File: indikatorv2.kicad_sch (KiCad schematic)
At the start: 61 parts, among them U1 XIAO-ESP32-C3-SMD

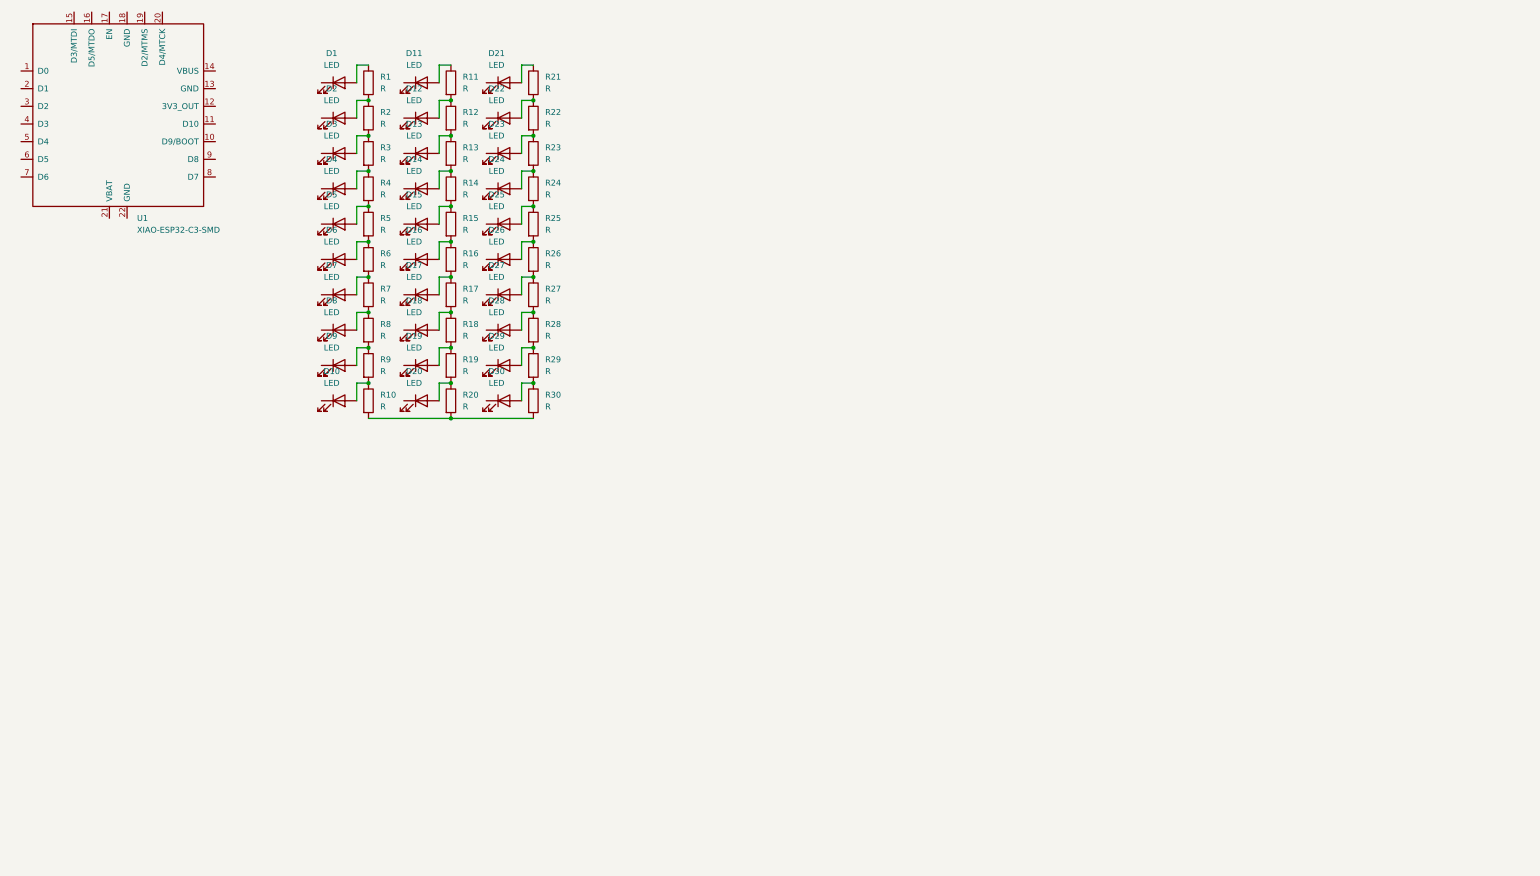
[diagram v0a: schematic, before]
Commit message: connect all leds and mosfets ig, still need to do all the battery stuff
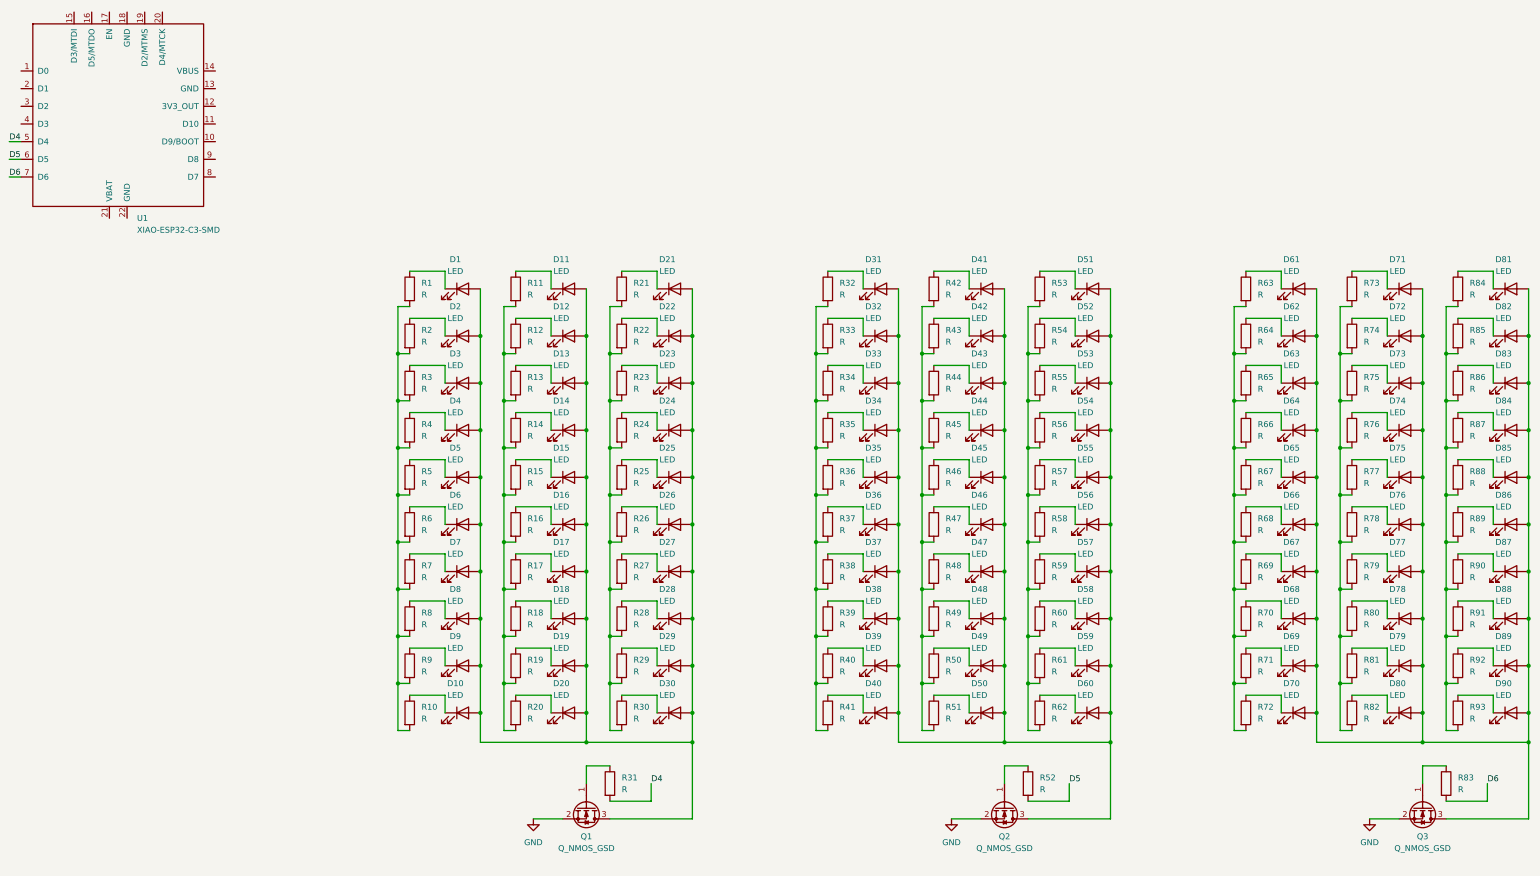
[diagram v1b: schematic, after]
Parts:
- added D31, D32, D33, D34, D35, D36, D37, D38, D39, D40, D41, D42, D43, D44, D45, D46, D47, D48, D49, D50, D51, D52, D53, D54, D55, D56, D57, D58, D59, D60, D61, D62, D63, D64, D65, D66, D67, D68, D69, D70, D71, D72, D73, D74, D75, D76, D77, D78, D79, D80, D81, D82, D83, D84, D85, D86, D87, D88, D89, D90: LED, LED_SMD:LED_Cree-XHP50_3V_HighDensity, symbol Device:LED
- added Q1, Q2, Q3: Q_NMOS_GSD, Converter_DCDC:Converter_DCDC_XP_POWER-IAxxxxD_THT, symbol Transistor_FET:Q_NMOS_GSD
- added R31, R32, R33, R34, R35, R36, R37, R38, R39, R40, R41, R42, R43, R44, R45, R46, R47, R48, R49, R50, R51, R52, R53, R54, R55, R56, R57, R58, R59, R60, R61, R62, R63, R64, R65, R66, R67, R68, R69, R70, R71, R72, R73, R74, R75, R76, R77, R78, R79, R80, R81, R82, R83, R84, R85, R86, R87, R88, R89, R90, R91, R92, R93: R, Package_BGA:UFBGA-64_5x5mm_Layout8x8_P0.5mm, symbol Device:R
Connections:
- net at D28.1 (K): now also R28.1
- net at D24.1 (K): now also R24.1
- net at D1.2 (A): now also D10.2 (A), D11.2 (A), D12.2 (A), D13.2 (A), D14.2 (A), D15.2 (A), D16.2 (A), D17.2 (A), D18.2 (A), D19.2 (A), D2.2 (A), D20.2 (A), D21.2 (A), D22.2 (A), D23.2 (A), D24.2 (A), D25.2 (A), D26.2 (A), D27.2 (A), D28.2 (A), D29.2 (A), D3.2 (A), D30.2 (A), D4.2 (A), D5.2 (A), D6.2 (A), D7.2 (A), D8.2 (A), D9.2 (A), Q1.3 (D); no longer R1.1
- net at D6.1 (K): now also R6.1
- net at D30.1 (K): now also R30.1
- net at D5.1 (K): now also R5.1
- net at D4.1 (K): now also R4.1
- net D4: now reaches U1.5 (D4)
- net D4: now also R31.2
- net D5: now reaches U1.6 (D5)
- net D5: now also R52.2
- net D6: now reaches U1.7 (D6)
- net D6: now also R83.2
- net at R21.1: now also D21.1 (K); no longer D21.2 (A)
- net at D9.1 (K): now also R9.1
- net at D3.1 (K): now also R3.1
- net at D1.1 (K): now also R1.1
- net at D19.1 (K): now also R19.1
- net at D11.1 (K): now also R11.1
- net at D22.1 (K): now also R22.1
- net at D23.1 (K): now also R23.1
- net at D26.1 (K): now also R26.1
- net at D8.1 (K): now also R8.1
- net at D20.1 (K): now also R20.1
- net at D2.1 (K): now also R2.1
- net at D7.1 (K): now also R7.1
- net at D17.1 (K): now also R17.1
- net at D27.1 (K): now also R27.1
- net at D15.1 (K): now also R15.1
- net at D13.1 (K): now also R13.1
- net at D18.1 (K): now also R18.1
- net at D12.1 (K): now also R12.1
- net at D29.1 (K): now also R29.1
- net at D14.1 (K): now also R14.1
- net at D16.1 (K): now also R16.1
- net at D25.1 (K): now also R25.1
- net at D10.1 (K): now also R10.1
- new net: D86.1 (K), R89.1
- new net: D61.2 (A), D62.2 (A), D63.2 (A), D64.2 (A), D65.2 (A), D66.2 (A), D67.2 (A), D68.2 (A), D69.2 (A), D70.2 (A), D71.2 (A), D72.2 (A), D73.2 (A), D74.2 (A), D75.2 (A), D76.2 (A), D77.2 (A), D78.2 (A), D79.2 (A), D80.2 (A), D81.2 (A), D82.2 (A), D83.2 (A), D84.2 (A), D85.2 (A), D86.2 (A), D87.2 (A), D88.2 (A), D89.2 (A), D90.2 (A), Q3.3 (D)
- new net: R11.2, R12.2, R13.2, R14.2, R15.2, R16.2, R17.2, R18.2, R19.2, R20.2
- new net: D43.1 (K), R44.1
- new net: R42.2, R43.2, R44.2, R45.2, R46.2, R47.2, R48.2, R49.2, R50.2, R51.2
- new net: D77.1 (K), R79.1
- new net: D44.1 (K), R45.1
- new net: D31.2 (A), D32.2 (A), D33.2 (A), D34.2 (A), D35.2 (A), D36.2 (A), D37.2 (A), D38.2 (A), D39.2 (A), D40.2 (A), D41.2 (A), D42.2 (A), D43.2 (A), D44.2 (A), D45.2 (A), D46.2 (A), D47.2 (A), D48.2 (A), D49.2 (A), D50.2 (A), D51.2 (A), D52.2 (A), D53.2 (A), D54.2 (A), D55.2 (A), D56.2 (A), D57.2 (A), D58.2 (A), D59.2 (A), D60.2 (A), Q2.3 (D)
- new net: D46.1 (K), R47.1
- new net: D34.1 (K), R35.1
- new net: D76.1 (K), R78.1
- new net: D58.1 (K), R60.1
- new net: R53.2, R54.2, R55.2, R56.2, R57.2, R58.2, R59.2, R60.2, R61.2, R62.2
- new net: R1.2, R10.2, R2.2, R3.2, R4.2, R5.2, R6.2, R7.2, R8.2, R9.2
- new net: D68.1 (K), R70.1
- new net: D57.1 (K), R59.1
- new net: D37.1 (K), R38.1
- new net: D87.1 (K), R90.1
- new net: D49.1 (K), R50.1
- new net: D32.1 (K), R33.1
- new net: D83.1 (K), R86.1
- new net: R84.2, R85.2, R86.2, R87.2, R88.2, R89.2, R90.2, R91.2, R92.2, R93.2
- new net: D75.1 (K), R77.1
- new net: R73.2, R74.2, R75.2, R76.2, R77.2, R78.2, R79.2, R80.2, R81.2, R82.2
- new net: D79.1 (K), R81.1
- new net: D72.1 (K), R74.1
- new net: R32.2, R33.2, R34.2, R35.2, R36.2, R37.2, R38.2, R39.2, R40.2, R41.2
- new net: D31.1 (K), R32.1
- new net: R21.2, R22.2, R23.2, R24.2, R25.2, R26.2, R27.2, R28.2, R29.2, R30.2
- new net: D47.1 (K), R48.1
- new net: D60.1 (K), R62.1
- new net: D78.1 (K), R80.1
- new net: D40.1 (K), R41.1
- new net: D45.1 (K), R46.1
- new net: D48.1 (K), R49.1
- new net: D33.1 (K), R34.1
- new net: D63.1 (K), R65.1
- new net: R63.2, R64.2, R65.2, R66.2, R67.2, R68.2, R69.2, R70.2, R71.2, R72.2
- new net: D50.1 (K), R51.1
- new net: D39.1 (K), R40.1
- new net: D70.1 (K), R72.1
- new net: D56.1 (K), R58.1
- new net: D74.1 (K), R76.1
- new net: D51.1 (K), R53.1
- new net: D53.1 (K), R55.1
- new net: D36.1 (K), R37.1
- new net: D85.1 (K), R88.1
- new net: D59.1 (K), R61.1
- new net: Q1.1 (G), R31.1
- new net: D61.1 (K), R63.1
- new net: D82.1 (K), R85.1
- new net: D66.1 (K), R68.1
- new net: D62.1 (K), R64.1
- new net: D41.1 (K), R42.1
- new net: D52.1 (K), R54.1
- new net: D84.1 (K), R87.1
- new net: D69.1 (K), R71.1
- new net: D64.1 (K), R66.1
- new net: D73.1 (K), R75.1
- new net: D65.1 (K), R67.1
- new net: D81.1 (K), R84.1
- new net: D35.1 (K), R36.1
- new net: D89.1 (K), R92.1
- new net: D42.1 (K), R43.1
- new net: D38.1 (K), R39.1
- new net: D54.1 (K), R56.1
- new net: Q3.1 (G), R83.1
- new net: D90.1 (K), R93.1
- new net: D55.1 (K), R57.1
- new net: D80.1 (K), R82.1
- new net: D71.1 (K), R73.1
- new net: D67.1 (K), R69.1
- new net: Q2.1 (G), R52.1
- new net: D88.1 (K), R91.1
- new net GND: Q1.2 (S), Q2.2 (S), Q3.2 (S)

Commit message: journal
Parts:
- added J1: Conn_01x02_Pin, symbol Connector:Conn_01x02_Pin
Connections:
- new net BAT+: J1.1 (Pin_1)
- new net BAT-: J1.2 (Pin_2)
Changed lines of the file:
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@@
 		)
 	)
+	(label "BAT-"
+		(at 106.68 52.07 0)
+		(effects
+			(font
+				(size 1.27 1.27)
+			)
+			(justify left bottom)
+		)
+	)
 	(label "D5"
 		(at 17.78 54.61 0)
@@
 		)
 	)
+	(label "BAT+"
+		(at 106.68 49.53 0)
+		(effects
+			(font
+				(size 1.27 1.27)
+			)
+			(justify left bottom)
+		)
+	)
 	(label "D6"
 		(at 336.55 189.23 0)
@@
 					(unit 1)
 				)
+			)
+		)
+	)
+	(symbol
+		(lib_id "Connector:Conn_01x02_Pin")
+		(at 101.6 49.53 0)
+		(unit 1)
+		(body_style 1)
+		(exclude_from_sim no)
+		(in_bom yes)
+		(on_board yes)
+		(in_pos_files yes)
+		(dnp no)
+		(fields_autoplaced yes)
+		(property "Reference" "J1"
+			(at 102.235 44.45 0)
+			(show_name no)
+			(do_not_autoplace no)
+			(effects
+				(font
+					(size 1.27 1.27)
+				)
+			)
+		)
+		(property "Value" "Conn_01x02_Pin"
+			(at 102.235 46.99 0)
+			(show_name no)
+			(do_not_autoplace no)
+			(effects
+				(font
+					(size 1.27 1.27)
+				)
+			)
+		)
+		(property "Footprint" ""
+			(at 101.6 49.53 0)
+			(hide yes)
+			(show_name no)
+			(do_not_autoplace no)
+			(effects
+				(font
+					(size 1.27 1.27)
+				)
+			)
+		)
+		(property "Datasheet" ""
+			(at 101.6 49.53 0)
+			(hide yes)
+			(show_name no)
+			(do_not_autoplace no)
+			(effects
+				(font
+					(size 1.27 1.27)
+				)
+			)
+		)
+		(property "Description" "Generic connector, single row, 01x02, script generated"
+			(at 101.6 49.53 0)
+			(hide yes)
+			(show_name no)
+			(do_not_autoplace no)
+			(effects
+				(font
+					(size 1.27 1.27)
+				)
+			)
+		)
+		(pin "2"
+		)
+		(pin "1"
+		)
+		(instances
+			(project "indikatorv2"
+				(path "/2add1593-661d-41a8-811f-b5b798956a46"
+					(reference "J1")
+					(unit 1)
+				)

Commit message: do battery stuff
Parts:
- removed R31, R52, R83: R, Package_BGA:UFBGA-64_5x5mm_Layout8x8_P0.5mm, symbol Device:R
- added F1: Fuse, symbol Device:Fuse
- added J2, J3, J4: Conn_01x02_Pin, symbol Connector:Conn_01x02_Pin
- added SW1: SW_SPST, Button_Switch_THT:SW_NKK_GW12LJP, symbol Switch:SW_SPST
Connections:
- net D4: now also Q1.1 (G)
- net D5: now also Q2.1 (G)
- net D6: now also Q3.1 (G)
- net GND: now also U1.22 (GND), J3.2 (Pin_2), J4.2 (Pin_2)
- net BOOST_OUT: now reaches D11.1 (K), R11.1
- net BOOST_OUT: now also D1.1 (K), D21.1 (K), D31.1 (K), D41.1 (K), D51.1 (K), D61.1 (K), D71.1 (K), D81.1 (K), R1.1, R21.1, R32.1, R42.1, R53.1, R63.1, R73.1, R84.1, U1.21 (VBAT), J4.1 (Pin_1)
- new net: F1.2, SW1.1 (A)
- new net BOOST_IN: J3.1 (Pin_1), SW1.2 (B)
- new net PROTECTED+: F1.1, J2.1 (Pin_1)
- new net PROTECTED-: J2.2 (Pin_2)
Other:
- moved on the sheet: D1, D10, D11, D12, D13, D14, D15, D16, D17, D18, D19, D2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

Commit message: create fuse footprint, assign footprints for everything and pass erc
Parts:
- F1: footprint (none) -> components:FuseHolder_ELCOM_PBF-4
- J1, J2, J3, J4: footprint (none) -> TerminalBlock:TerminalBlock_MaiXu_MX126-5.0-02P_1x02_P5.00mm
- R1, R10, R11, R12, R13, R14, R15, R16, R17, R18, R19, R2, R20, R21, R22, R23, R24, R25, R26, R27, R28, R29, R3, R30, R4, R5, R6, R63, R64, R65, R66, R67, R68, R69, R7, R70, R71, R72, R73, R74, R75, R76, R77, R78, R79, R8, R80, R81, R82, R84, R85, R86, R87, R88, R89, R9, R90, R91, R92, R93: value R -> 200; footprint Package_BGA:UFBGA-64_5x5mm_Layout8x8_P0.5mm -> Resistor_SMD:R_0805_2012Metric
- R32, R33, R34, R35, R36, R37, R38, R39, R40, R41, R42, R43, R44, R45, R46, R47, R48, R49, R50, R51, R53, R54, R55, R56, R57, R58, R59, R60, R61, R62: value R -> 300; footprint Package_BGA:UFBGA-64_5x5mm_Layout8x8_P0.5mm -> Resistor_SMD:R_0805_2012Metric
- U1: footprint Seeed_Studio_XIAO_Series:XIAO-ESP32-C3-SMD -> RF_Module:MCU_Seeed_ESP32C3
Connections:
- no-connect marks 0 -> 17
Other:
- moved on the sheet: U1

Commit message: i tried okay, also journal
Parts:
- D1, D10, D11, D12, D13, D14, D15, D16, D17, D18, D19, D2, D20, D21, D22, D23, D24, D25, D26, D27, D28, D29, D3, D30, D31, D32, D33, D34, D35, D36, D37, D38, D39, D4, D40, D41, D42, D43, D44, D45, D46, D47, D48, D49, D5, D50, D51, D52, D53, D54, D55, D56, D57, D58, D59, D6, D60, D61, D62, D63, D64, D65, D66, D67, D68, D69, D7, D70, D71, D72, D73, D74, D75, D76, D77, D78, D79, D8, D80, D81, D82, D83, D84, D85, D86, D87, D88, D89, D9, D90: footprint LED_SMD:LED_Cree-XHP50_3V_HighDensity -> components:L128-CLR1003500000
